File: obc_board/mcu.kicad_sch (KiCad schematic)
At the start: 47 parts, among them J17 Micro_SD_Card, U19 STM32L552ZET6Q, Y3 8MHz, Y4 32.768kHz

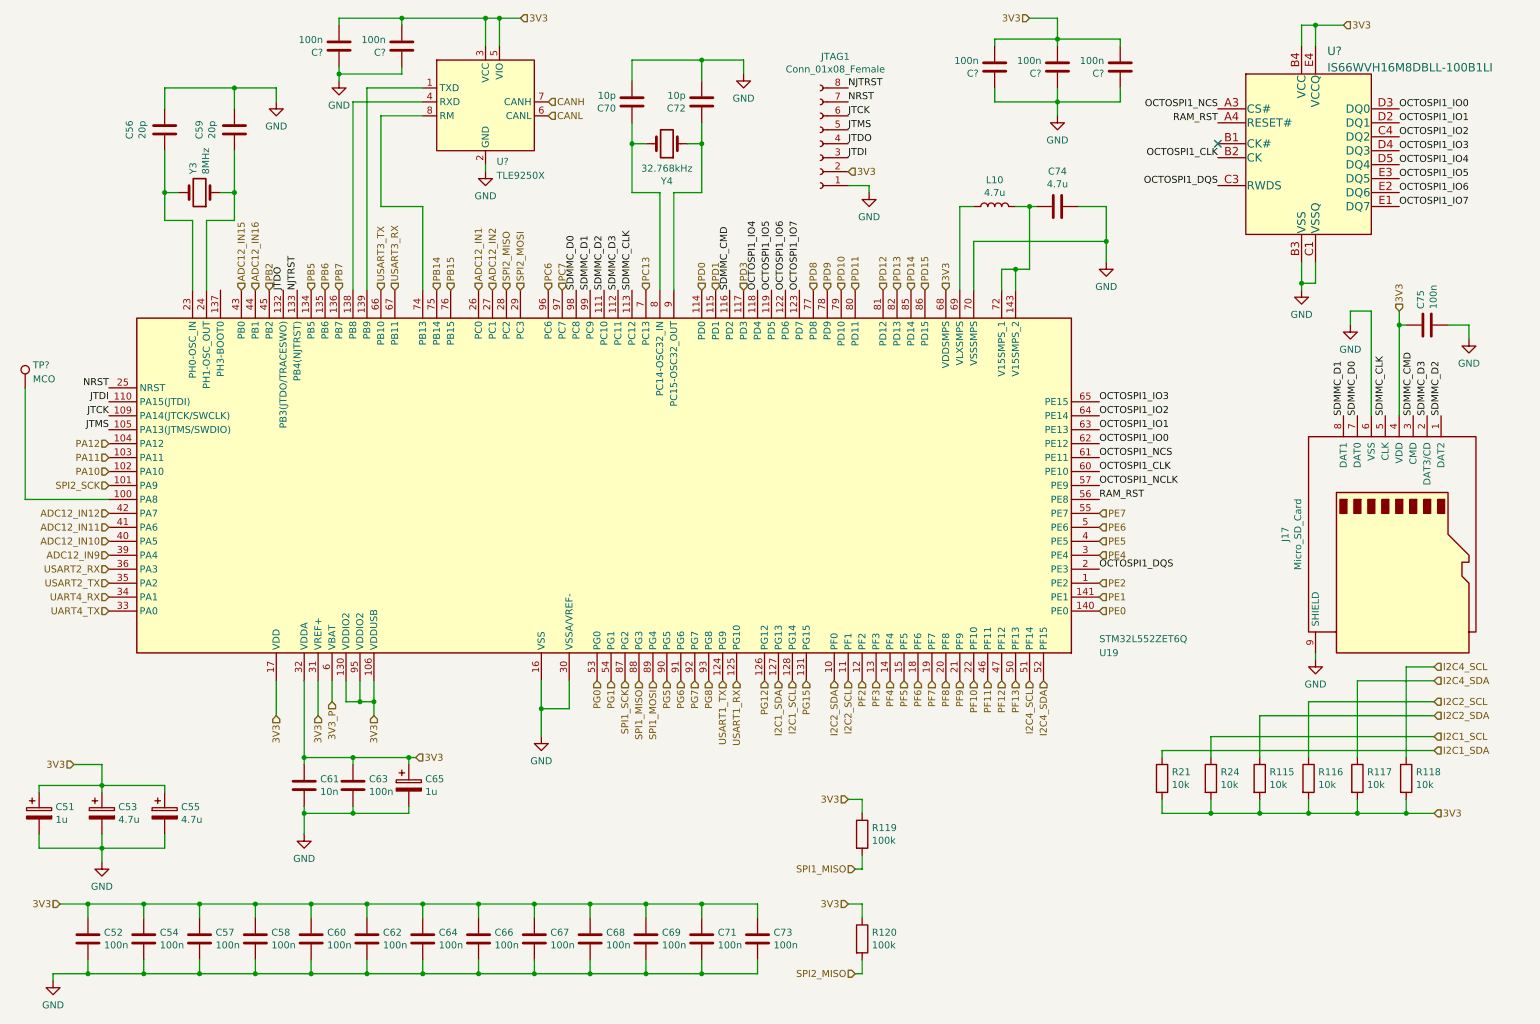
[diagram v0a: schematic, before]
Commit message: changed magnetorquer driver IC and changed power switch IC
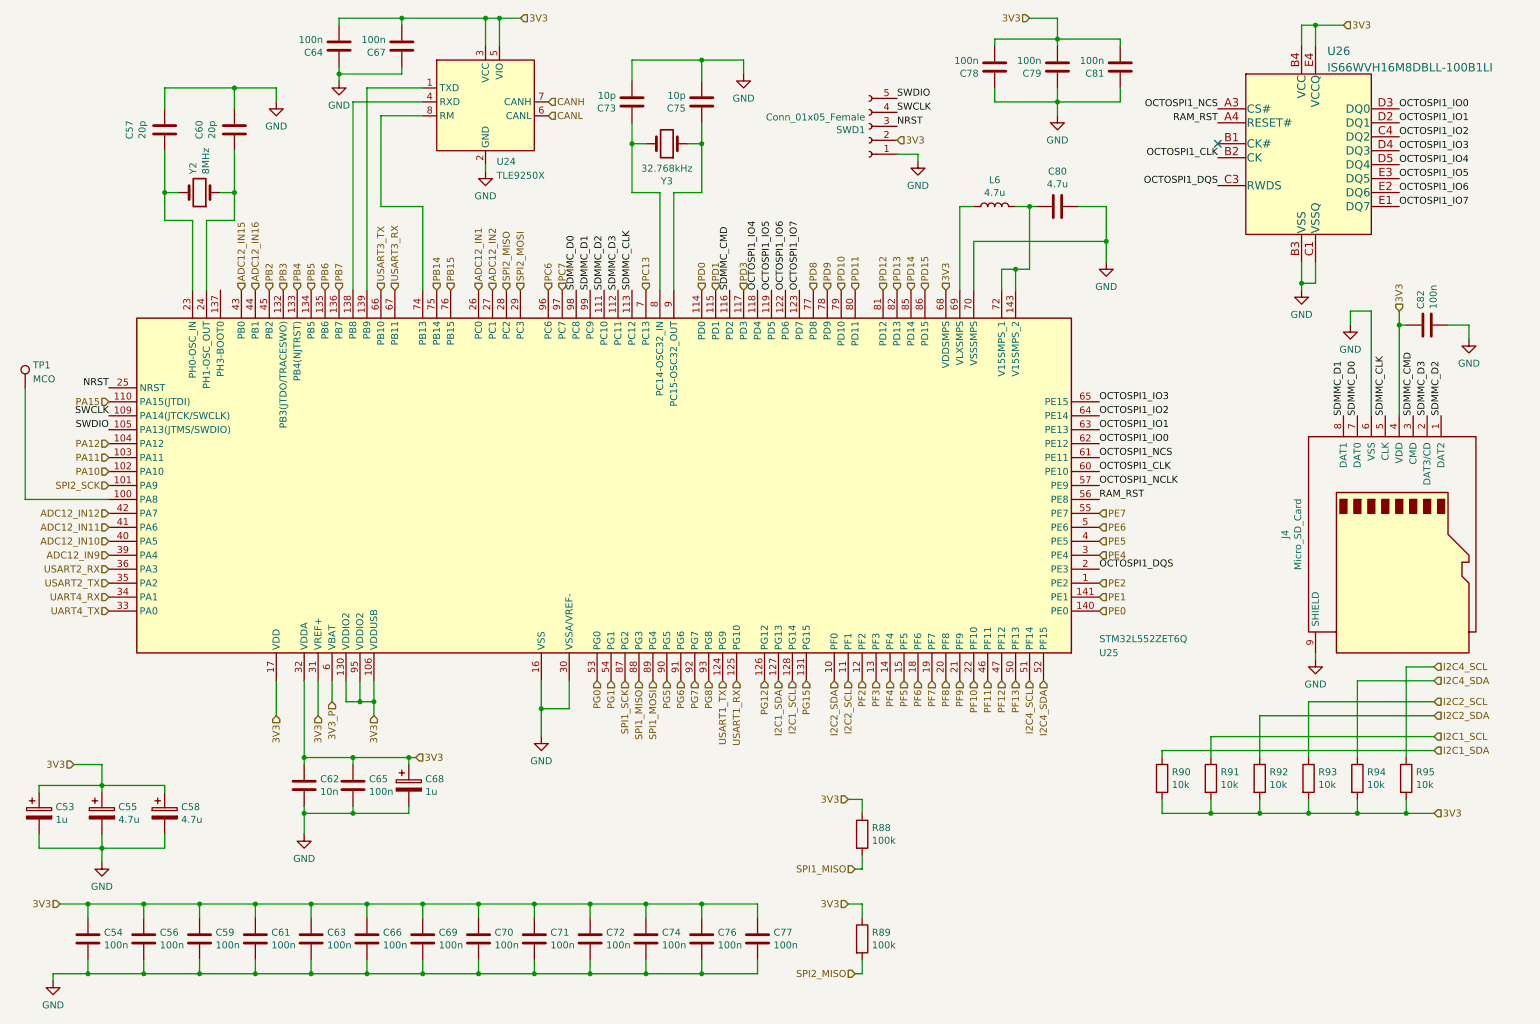
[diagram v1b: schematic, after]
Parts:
- removed JTAG1: Conn_01x08_Female, Connector_Molex:Molex_PicoBlade_53261-0871_1x08-1MP_P1.25mm_Horizontal, symbol Connector:Conn_01x08_Female
- added SWD1: Conn_01x05_Female, Connector_Molex:Molex_PicoBlade_53261-0571_1x05-1MP_P1.25mm_Horizontal, symbol Connector:Conn_01x05_Female
- gave numbers to parts that had none: 8
- renumbered C51 to C53, C52 to C54, C53 to C55, C54 to C56, C56 to C57, C55 to C58, C57 to C59, C59 to C60, C58 to C61, C61 to C62, C60 to C63, C63 to C65, C62 to C66, C65 to C68, C64 to C69, C66 to C70, C67 to C71, C68 to C72, C70 to C73, C69 to C74, C72 to C75, C71 to C76, C73 to C77, C74 to C80, C75 to C82, J17 to J4, L10 to L6, R119 to R88, R120 to R89, R21 to R90, R24 to R91, R115 to R92, R116 to R93, R117 to R94, R118 to R95, U19 to U25, Y3 to Y2, Y4 to Y3
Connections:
- net GND: now also SWD1.1 (Pin_1)
- net NRST: now also SWD1.3 (Pin_3)
- net VCCQ: now also SWD1.2 (Pin_2)
- net JTCK renamed SWCLK
- net SWCLK: now also SWD1.4 (Pin_4)
- net JTDI renamed PA15
- net JTDO renamed PB3
- net JTMS renamed SWDIO
- net SWDIO: now also SWD1.5 (Pin_5)
- net NJTRST renamed PB4

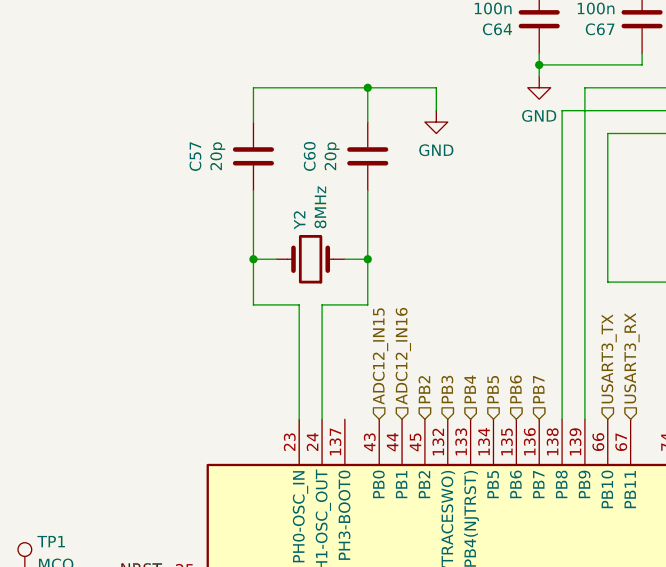
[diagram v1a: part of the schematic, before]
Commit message: updated digikey part numbers and footprints
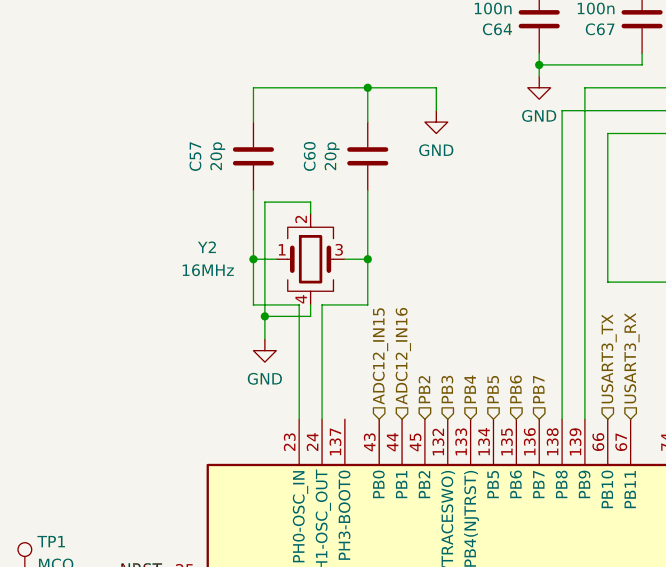
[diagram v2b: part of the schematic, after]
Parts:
- removed Y2: 8MHz, Crystal:Crystal_SMD_3225-4Pin_3.2x2.5mm, symbol Device:Crystal
- added Y2: 16MHz, Crystal:Crystal_SMD_3225-4Pin_3.2x2.5mm, symbol Device:Crystal_GND24
- C53, C68: Digikey Part Number 311-1446-2-ND -> 399-17713-1-ND
- C54, C56, C59, C61, C63, C64, C65, C66, C67, C69, C70, C71, C72, C74, C76, C77, C78, C79, C81, C82: Digikey Part Number 490-16433-1-ND -> 399-6828-1-ND
- C55, C58: Digikey Part Number 490-9618-1-ND -> 399-15711-1-ND
- C57, C60: footprint Capacitor_SMD:C_0201_0603Metric -> Capacitor_SMD:C_0603_1608Metric; Digikey Part Number 490-9618-1-ND -> 399-C0603C200K4HACAUTOCT-ND
- C62: footprint Capacitor_SMD:C_0805_2012Metric -> Capacitor_SMD:C_0603_1608Metric; Digikey Part Number 490-8295-1-ND -> 399-14104-1-ND
- C73, C75: footprint Capacitor_SMD:C_0201_0603Metric -> Capacitor_SMD:C_0402_1005Metric; Digikey Part Number 490-7750-1-ND -> 399-C0402C100J5HACAUTOCT-ND
- C80: footprint Capacitor_SMD:C_0201_0603Metric -> Capacitor_SMD:C_0805_2012Metric; Digikey Part Number 490-9618-1-ND -> 399-15711-1-ND
- R88, R89: Digikey Part Number YAG2307CT-ND -> YAG3434CT-ND
- R90, R91, R92, R93, R94, R95: Digikey Part Number 311-10.0KLRCT-ND -> YAG3436CT-ND
- SWD1: Digikey Part Number WM7623CT-ND -> WM26499CT-ND
- TP1: footprint (none) -> TestPoint:TestPoint_Pad_D1.5mm
- U24: footprint (none) -> Package_DFN_QFN:DFN-8-1EP_3x3mm_P0.65mm_EP1.55x2.4mm; Digikey Part Number (none) -> 448-TLE9250XLEXUMA1CT-ND
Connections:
- net GND: now also Y2.2, Y2.4
- net at C60.1, U25.24 (PH1-OSC_OUT): now also Y2.3
- net at C57.1, U25.23 (PH0-OSC_IN): now also Y2.1

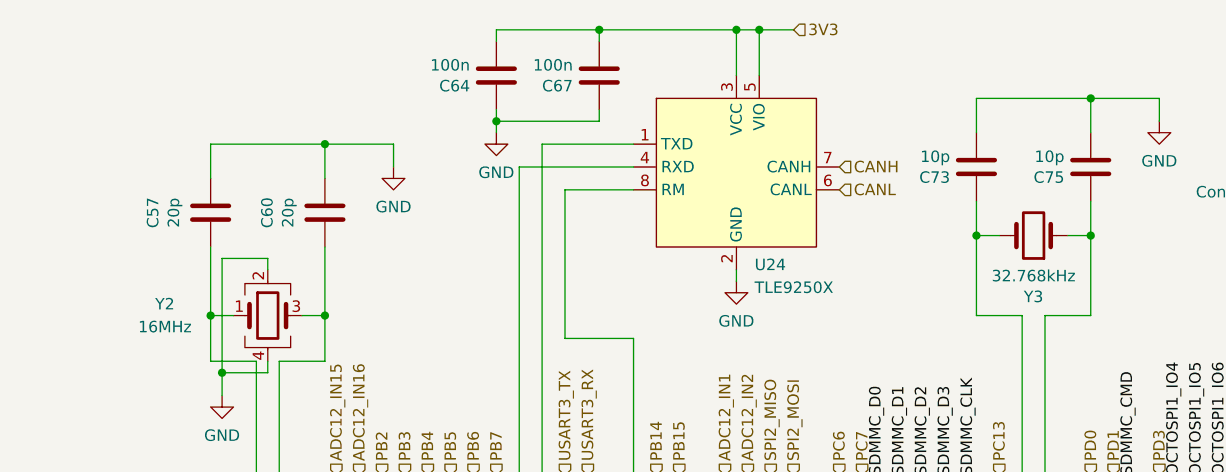
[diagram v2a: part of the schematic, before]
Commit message: updated load capacitances
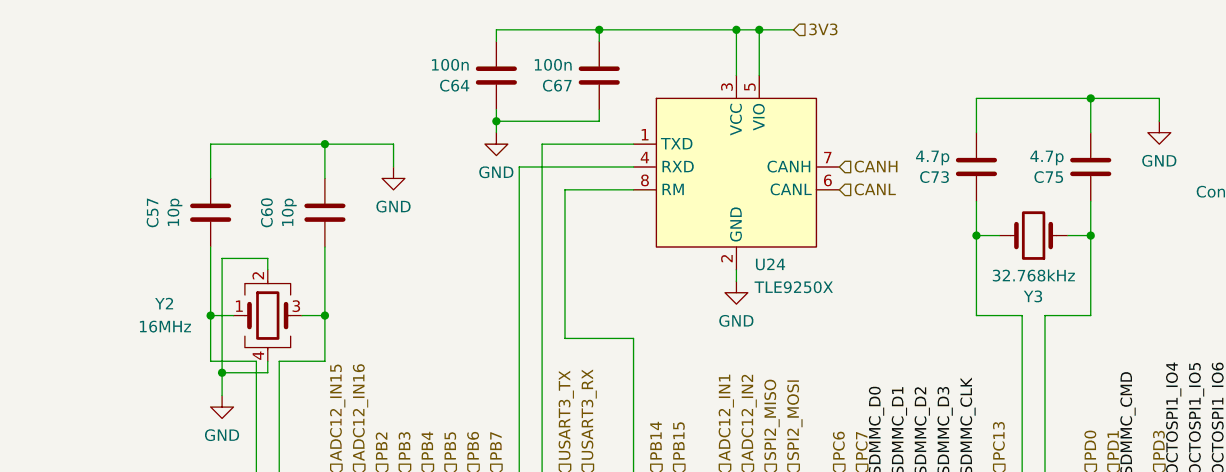
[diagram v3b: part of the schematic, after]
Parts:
- C57, C60: value 20p -> 10p; footprint Capacitor_SMD:C_0603_1608Metric -> Capacitor_SMD:C_0402_1005Metric; Digikey Part Number 399-C0603C200K4HACAUTOCT-ND -> 399-C0402C100J5HACAUTOCT-ND
- C73, C75: value 10p -> 4.7p; Digikey Part Number 399-C0402C100J5HACAUTOCT-ND -> 399-17559-1-ND
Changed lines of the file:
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@@
       (effects (font (size 1.27 1.27)) (justify left))
     )
-    (property "Value" "10p" (id 1) (at 135.509 29.337 0)
+    (property "Value" "4.7p" (id 1) (at 135.509 29.337 0)
       (effects (font (size 1.27 1.27)) (justify left))
     )
@@
       (effects (font (size 1.27 1.27)) hide)
     )
-    (property "Digikey Part Number" "399-C0402C100J5HACAUTOCT-ND" (id 4) (at 138.43 30.48 0)
+    (property "Digikey Part Number" "399-17559-1-ND" (id 4) (at 138.43 30.48 0)
       (effects (font (size 1.27 1.27)) hide)
     )
@@
       (effects (font (size 1.27 1.27)) (justify left))
     )
-    (property "Value" "10p" (id 1) (at 122.809 29.337 0)
+    (property "Value" "4.7p" (id 1) (at 122.809 29.337 0)
       (effects (font (size 1.27 1.27)) (justify left))
     )
@@
       (effects (font (size 1.27 1.27)) hide)
     )
-    (property "Digikey Part Number" "399-C0402C100J5HACAUTOCT-ND" (id 4) (at 125.73 30.48 0)
+    (property "Digikey Part Number" "399-17559-1-ND" (id 4) (at 125.73 30.48 0)
       (effects (font (size 1.27 1.27)) hide)
     )
@@
     (in_bom yes) (on_board yes)
     (property "Reference" "C60" (id 0) (at 46.9392 35.56 90))
-    (property "Value" "20p" (id 1) (at 49.2506 35.56 90))
-    (property "Footprint" "Capacitor_SMD:C_0603_1608Metric" (id 2) (at 52.3748 31.75 0)
+    (property "Value" "10p" (id 1) (at 49.2506 35.56 90))
+    (property "Footprint" "Capacitor_SMD:C_0402_1005Metric" (id 2) (at 52.3748 31.75 0)
       (effects (font (size 1.27 1.27)) hide)
     )
@@
       (effects (font (size 1.27 1.27)) hide)
     )
-    (property "Digikey Part Number" "399-C0603C200K4HACAUTOCT-ND" (id 4) (at 53.34 35.56 0)
+    (property "Digikey Part Number" "399-C0402C100J5HACAUTOCT-ND" (id 4) (at 53.34 35.56 0)
       (effects (font (size 1.27 1.27)) hide)
     )
@@
     (in_bom yes) (on_board yes)
     (property "Reference" "C57" (id 0) (at 34.2392 35.56 90))
-    (property "Value" "20p" (id 1) (at 36.5506 35.56 90))
-    (property "Footprint" "Capacitor_SMD:C_0603_1608Metric" (id 2) (at 39.6748 31.75 0)
+    (property "Value" "10p" (id 1) (at 36.5506 35.56 90))
+    (property "Footprint" "Capacitor_SMD:C_0402_1005Metric" (id 2) (at 39.6748 31.75 0)
       (effects (font (size 1.27 1.27)) hide)
     )
@@
       (effects (font (size 1.27 1.27)) hide)
     )
-    (property "Digikey Part Number" "399-C0603C200K4HACAUTOCT-ND" (id 4) (at 40.64 35.56 0)
+    (property "Digikey Part Number" "399-C0402C100J5HACAUTOCT-ND" (id 4) (at 40.64 35.56 0)
       (effects (font (size 1.27 1.27)) hide)
     )

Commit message: updated pcb
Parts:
- U26: footprint TFBGA24_6X8_ISI -> cubesat_obc:TFBGA24_5X5_6X8
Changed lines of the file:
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@@
       (effects (font (size 1.524 1.524)) (justify left))
     )
-    (property "Footprint" "TFBGA24_6X8_ISI" (id 2) (at 265.43 24.13 0)
+    (property "Footprint" "cubesat_obc:TFBGA24_5X5_6X8" (id 2) (at 265.43 24.13 0)
       (effects (font (size 1.524 1.524)) hide)
     )
